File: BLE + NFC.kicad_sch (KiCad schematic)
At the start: 1 part, among them IC5 nRF52832-CIAA-G-R7

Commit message: added buck
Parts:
- added JP1: SolderJumper_3_Open, symbol Jumper:SolderJumper_3_Open
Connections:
- net at IC5.A7 (VDD_1): now also IC5.H7 (VDD_2), JP1.2 (C)
- new net +1V8: JP1.3 (B)
- new net +3V3: JP1.1 (A)
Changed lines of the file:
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@@
   (junction (at 143.51 144.78) (diameter 0) (color 0 0 0 0)
   )
+  (junction (at 133.35 43.18) (diameter 0) (color 0 0 0 0)
+  )
   (junction (at 151.13 144.78) (diameter 0) (color 0 0 0 0)
   )
+  (wire (pts (xy 138.43 36.83) (xy 146.05 36.83))
+    (stroke (width 0) (type default))
+  )
   (wire (pts (xy 151.13 142.24) (xy 151.13 144.78))
     (stroke (width 0) (type default))
@@
     (stroke (width 0) (type default))
   )
+  (wire (pts (xy 135.89 43.18) (xy 135.89 45.72))
+    (stroke (width 0) (type default))
+  )
   (wire (pts (xy 143.51 144.78) (xy 143.51 147.32))
     (stroke (width 0) (type default))
   )
+  (wire (pts (xy 128.27 36.83) (xy 120.65 36.83))
+    (stroke (width 0) (type default))
+  )
+  (wire (pts (xy 146.05 26.67) (xy 146.05 36.83))
+    (stroke (width 0) (type default))
+  )
+  (wire (pts (xy 133.35 45.72) (xy 133.35 43.18))
+    (stroke (width 0) (type default))
+  )
   (wire (pts (xy 151.13 144.78) (xy 153.67 144.78))
     (stroke (width 0) (type default))
   )
+  (wire (pts (xy 120.65 26.67) (xy 120.65 36.83))
+    (stroke (width 0) (type default))
+  )
   (wire (pts (xy 153.67 142.24) (xy 153.67 144.78))
     (stroke (width 0) (type default))
   )
+  (wire (pts (xy 133.35 43.18) (xy 135.89 43.18))
+    (stroke (width 0) (type default))
+  )
   (wire (pts (xy 146.05 142.24) (xy 146.05 144.78))
+    (stroke (width 0) (type default))
+  )
+  (wire (pts (xy 133.35 40.64) (xy 133.35 43.18))
     (stroke (width 0) (type default))
   )
@@
         )
         (path "/017c50c6-333c-4d31-ad5a-278994a09b14/3720f3b4-03b0-4b33-b5d9-366640292599"
-          (reference "IC5") (unit 1)
+          (reference "IC6") (unit 1)
         )
       )
@@
   (symbol (lib_id "power:GND") (at 143.51 147.32 0) (unit 1)
     (in_bom yes) (on_board yes) (dnp no) (fields_autoplaced)
-    (property "Reference" "#PWR042" (at 143.51 153.67 0)
+    (property "Reference" "#PWR044" (at 143.51 153.67 0)
       (effects (font (size 1.27 1.27)) hide)
     )
@@
       (project "armband"
         (path "/017c50c6-333c-4d31-ad5a-278994a09b14/3720f3b4-03b0-4b33-b5d9-366640292599"
-          (reference "#PWR042") (unit 1)
-        )
-      )
+          (reference "#PWR044") (unit 1)
+        )
+      )
+    )
+  )
+  (symbol (lib_id "power:+1V8") (at 146.05 26.67 0) (unit 1)
+    (in_bom yes) (on_board yes) (dnp no) (fields_autoplaced)
+    (property "Reference" "#PWR014" (at 146.05 30.48 0)
+      (effects (font (size 1.27 1.27)) hide)
+    )
+    (property "Value" "+1V8" (at 146.05 22.86 0)
+      (effects (font (size 1.27 1.27)))
+    )
+    (property "Footprint" "" (at 146.05 26.67 0)
+      (effects (font (size 1.27 1.27)) hide)
+    )
+    (property "Datasheet" "" (at 146.05 26.67 0)
+      (effects (font (size 1.27 1.27)) hide)
+    )
+    (pin "1")
+    (instances
+      (project "armband"
+        (path "/017c50c6-333c-4d31-ad5a-278994a09b14/2935dd4b-68c9-428b-bdab-ba656d5b03fa"
+          (reference "#PWR014") (unit 1)
+        )
+        (path "/017c50c6-333c-4d31-ad5a-278994a09b14/3720f3b4-03b0-4b33-b5d9-366640292599"
+          (reference "#PWR051") (unit 1)
+        )
+      )
+    )
+  )
+  (symbol (lib_id "power:+3V3") (at 120.65 26.67 0) (unit 1)
+    (in_bom yes) (on_board yes) (dnp no) (fields_autoplaced)
+    (property "Reference" "#PWR019" (at 120.65 30.48 0)
+      (effects (font (size 1.27 1.27)) hide)
+    )
+    (property "Value" "+3V3" (at 120.65 22.86 0)
+      (effects (font (size 1.27 1.27)))
+    )
+    (property "Footprint" "" (at 120.65 26.67 0)
+      (effects (font (size 1.27 1.27)) hide)
+    )
+    (property "Datasheet" "" (at 120.65 26.67 0)
+      (effects (font (size 1.27 1.27)) hide)
+    )
+    (pin "1")
+    (instances
+      (project "armband"
+        (path "/017c50c6-333c-4d31-ad5a-278994a09b14/2935dd4b-68c9-428b-bdab-ba656d5b03fa"
+          (reference "#PWR019") (unit 1)
+        )
+        (path "/017c50c6-333c-4d31-ad5a-278994a09b14/3720f3b4-03b0-4b33-b5d9-366640292599"
+          (reference "#PWR017") (unit 1)
+        )
+      )
+    )
+  )
+  (symbol (lib_id "Jumper:SolderJumper_3_Open") (at 133.35 36.83 0) (unit 1)
+    (in_bom yes) (on_board yes) (dnp no) (fields_autoplaced)
+    (property "Reference" "JP1" (at 133.35 31.75 0)
+      (effects (font (size 1.27 1.27)))
+    )
+    (property "Value" "SolderJumper_3_Open" (at 133.35 34.29 0)
+      (effects (font (size 1.27 1.27)))
+    )
+    (property "Footprint" "" (at 133.35 36.83 0)
+      (effects (font (size 1.27 1.27)) hide)
+    )
+    (property "Datasheet" "~" (at 133.35 36.83 0)
+      (effects (font (size 1.27 1.27)) hide)
+    )
+    (pin "1")
+    (pin "2")
+    (pin "3")
+    (instances
+      (project "armband"
+        (path "/017c50c6-333c-4d31-ad5a-278994a09b14/2935dd4b-68c9-428b-bdab-ba656d5b03fa"
+          (reference "JP1") (unit 1)
+        )
+        (path "/017c50c6-333c-4d31-ad5a-278994a09b14/3720f3b4-03b0-4b33-b5d9-366640292599"
+          (reference "JP2") (unit 1)
+        )
+      )

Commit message: cleaned up symbol fields table and removed unused or duplicate fields.
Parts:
- IC5: MFN (none) -> 949-NRF52832CIAAG-R7; Manufacturer_Name Nordic Semiconductor -> (none); Manufacturer_Part_Number nRF52832-CIAA-G-R7 -> (none); Mouser Part Number 949-NRF52832CIAAG-R7 -> (none); Mouser Price/Stock https://www.mouser.co.uk/ProductDetail/Nordic-Semiconductor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 -> (none)
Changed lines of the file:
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@@
       (effects (font (size 1.27 1.27)) (justify left top) hide)
     )
-    (property "Mouser Part Number" "949-NRF52832CIAAG-R7" (at 172.72 566.04 0)
-      (effects (font (size 1.27 1.27)) (justify left top) hide)
-    )
-    (property "Mouser Price/Stock" "https://www.mouser.co.uk/ProductDetail/Nordic-Semiconductor/nRF52832-CIAA-G-R7?qs=TCDPyi3sCW0%252B18bmEBENMQ%3D%3D" (at 172.72 666.04 0)
-      (effects (font (size 1.27 1.27)) (justify left top) hide)
-    )
-    (property "Manufacturer_Name" "Nordic Semiconductor" (at 172.72 766.04 0)
-      (effects (font (size 1.27 1.27)) (justify left top) hide)
-    )
-    (property "Manufacturer_Part_Number" "nRF52832-CIAA-G-R7" (at 172.72 866.04 0)
-      (effects (font (size 1.27 1.27)) (justify left top) hide)
+    (property "MFN" "949-NRF52832CIAAG-R7" (at 120.65 71.12 0)
+      (effects (font (size 1.27 1.27)) hide)
     )
     (pin "A1")
@@
         )
         (path "/017c50c6-333c-4d31-ad5a-278994a09b14/3720f3b4-03b0-4b33-b5d9-366640292599"
-          (reference "IC6") (unit 1)
+          (reference "IC9") (unit 1)
         )
       )
@@
   (symbol (lib_id "power:GND") (at 143.51 147.32 0) (unit 1)
     (in_bom yes) (on_board yes) (dnp no) (fields_autoplaced)
-    (property "Reference" "#PWR044" (at 143.51 153.67 0)
+    (property "Reference" "#PWR067" (at 143.51 153.67 0)
       (effects (font (size 1.27 1.27)) hide)
     )
@@
       (project "armband"
         (path "/017c50c6-333c-4d31-ad5a-278994a09b14/3720f3b4-03b0-4b33-b5d9-366640292599"
-          (reference "#PWR044") (unit 1)
+          (reference "#PWR067") (unit 1)
         )
       )
@@
         )
         (path "/017c50c6-333c-4d31-ad5a-278994a09b14/3720f3b4-03b0-4b33-b5d9-366640292599"
-          (reference "#PWR051") (unit 1)
+          (reference "#PWR066") (unit 1)
         )
       )
@@
         )
         (path "/017c50c6-333c-4d31-ad5a-278994a09b14/3720f3b4-03b0-4b33-b5d9-366640292599"
-          (reference "#PWR017") (unit 1)
+          (reference "#PWR065") (unit 1)
         )
       )

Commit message: Add nRF base layout
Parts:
- added C25 (x2): 100n 16V, Capacitor_SMD:C_0402_1005Metric, symbol Device:C_Small
- added C25 (x2): 12pF, Capacitor_SMD:C_0402_1005Metric, symbol Device:C_Small
- added C25 (x2): 100pF, Capacitor_SMD:C_0402_1005Metric, symbol Device:C_Small
- added C8: 4u7 6.3V, Capacitor_SMD:C_0402_1005Metric, symbol Device:C_Small
- added C8: 1u 6.3V, Capacitor_SMD:C_0201_0603Metric, symbol Device:C_Small
- added L4, L6: 10uH, symbol Device:L_Small
- added L5: 15uH, symbol Device:L_Small
- added Y1: Crystal, symbol Device:Crystal
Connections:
- net GND: now also C25.2, C25.2, C25.2, C25.2, C8.1, C8.2
- net at IC5.A1 (XC2): now also C25.1
- net DEC2: now reaches IC5.A2 (DEC2)
- net DEC2: now also C25.1
- net DEC4: now reaches IC5.A6 (DEC4)
- net DEC4: now also C8.1, L5.1
- net at IC5.A7 (VDD_1), IC5.H7 (VDD_2), JP1.2 (C): now also C25.1, C8.2
- net at IC5.B2 (XC1): now also C25.2
- net at IC5.B6 (DCC): now also L4.2
- net at IC5.B7 (DEC1): now also C25.1
- net DEC3: now reaches IC5.C2 (DEC3)
- net DEC3: now also C25.1
- net BT_ANT: now reaches IC5.D1 (ANT)
- net BT_ANT: now also L6.1
- net NFC_ANT2: now reaches IC5.G5 (NFC2_/P0.10)
- net NFC_ANT1: now reaches IC5.G6 (NFC1/P0.09)
- new net: C25.2, Y1.1
- new net: C25.1, Y1.2
- new net: L4.1, L5.2

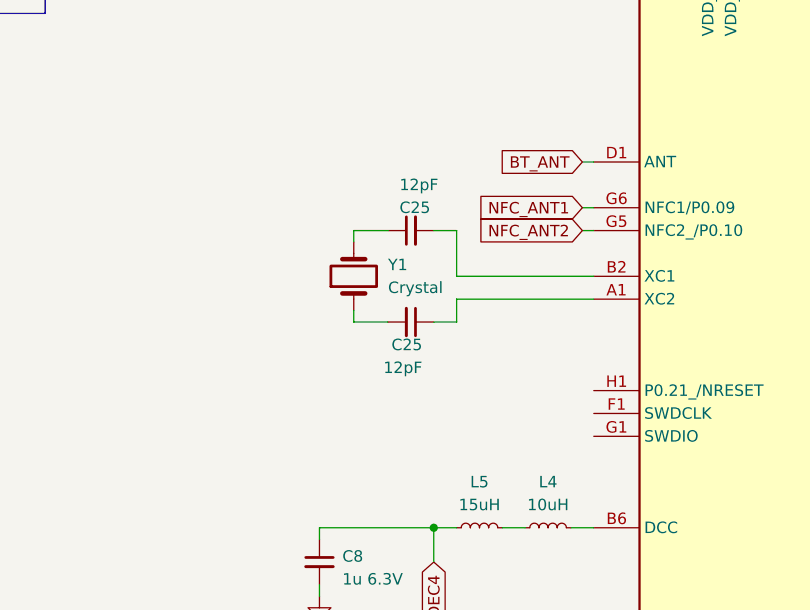
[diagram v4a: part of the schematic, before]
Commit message: added XTAL to nrf chip
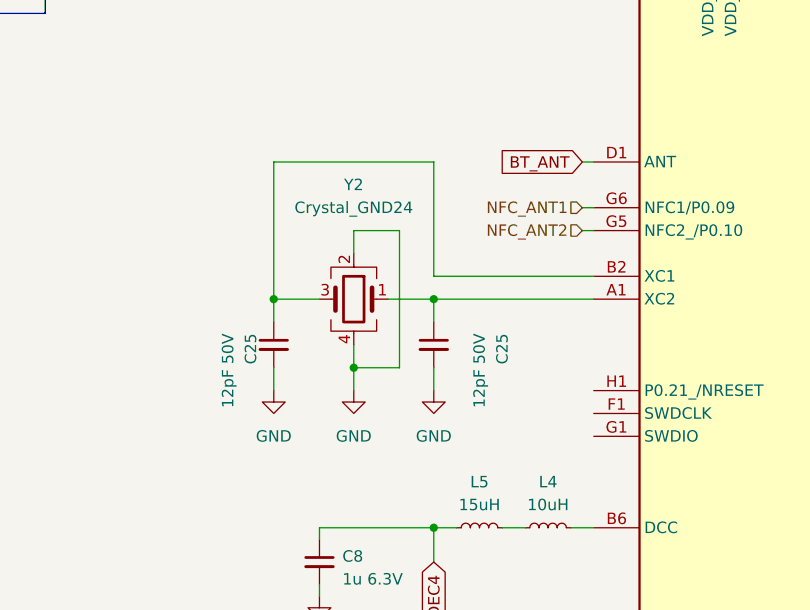
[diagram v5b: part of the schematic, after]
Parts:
- removed Y1: Crystal, symbol Device:Crystal
- added Y2: Crystal_GND24, ARMband:CX2016SA, symbol Device:Crystal_GND24
- C25: value 12pF -> 12pF 50V; footprint Capacitor_SMD:C_0402_1005Metric -> Capacitor_SMD:C_0201_0603Metric; MFN (none) -> 603-AC0201JNPO9BN120
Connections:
- net GND: now also C25.2, C25.2, Y2.2, Y2.4
- net at C25.1: now also IC5.B2 (XC1), Y2.3
- net at C25.1, IC5.A1 (XC2): now also Y2.1
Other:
- moved on the sheet: C25

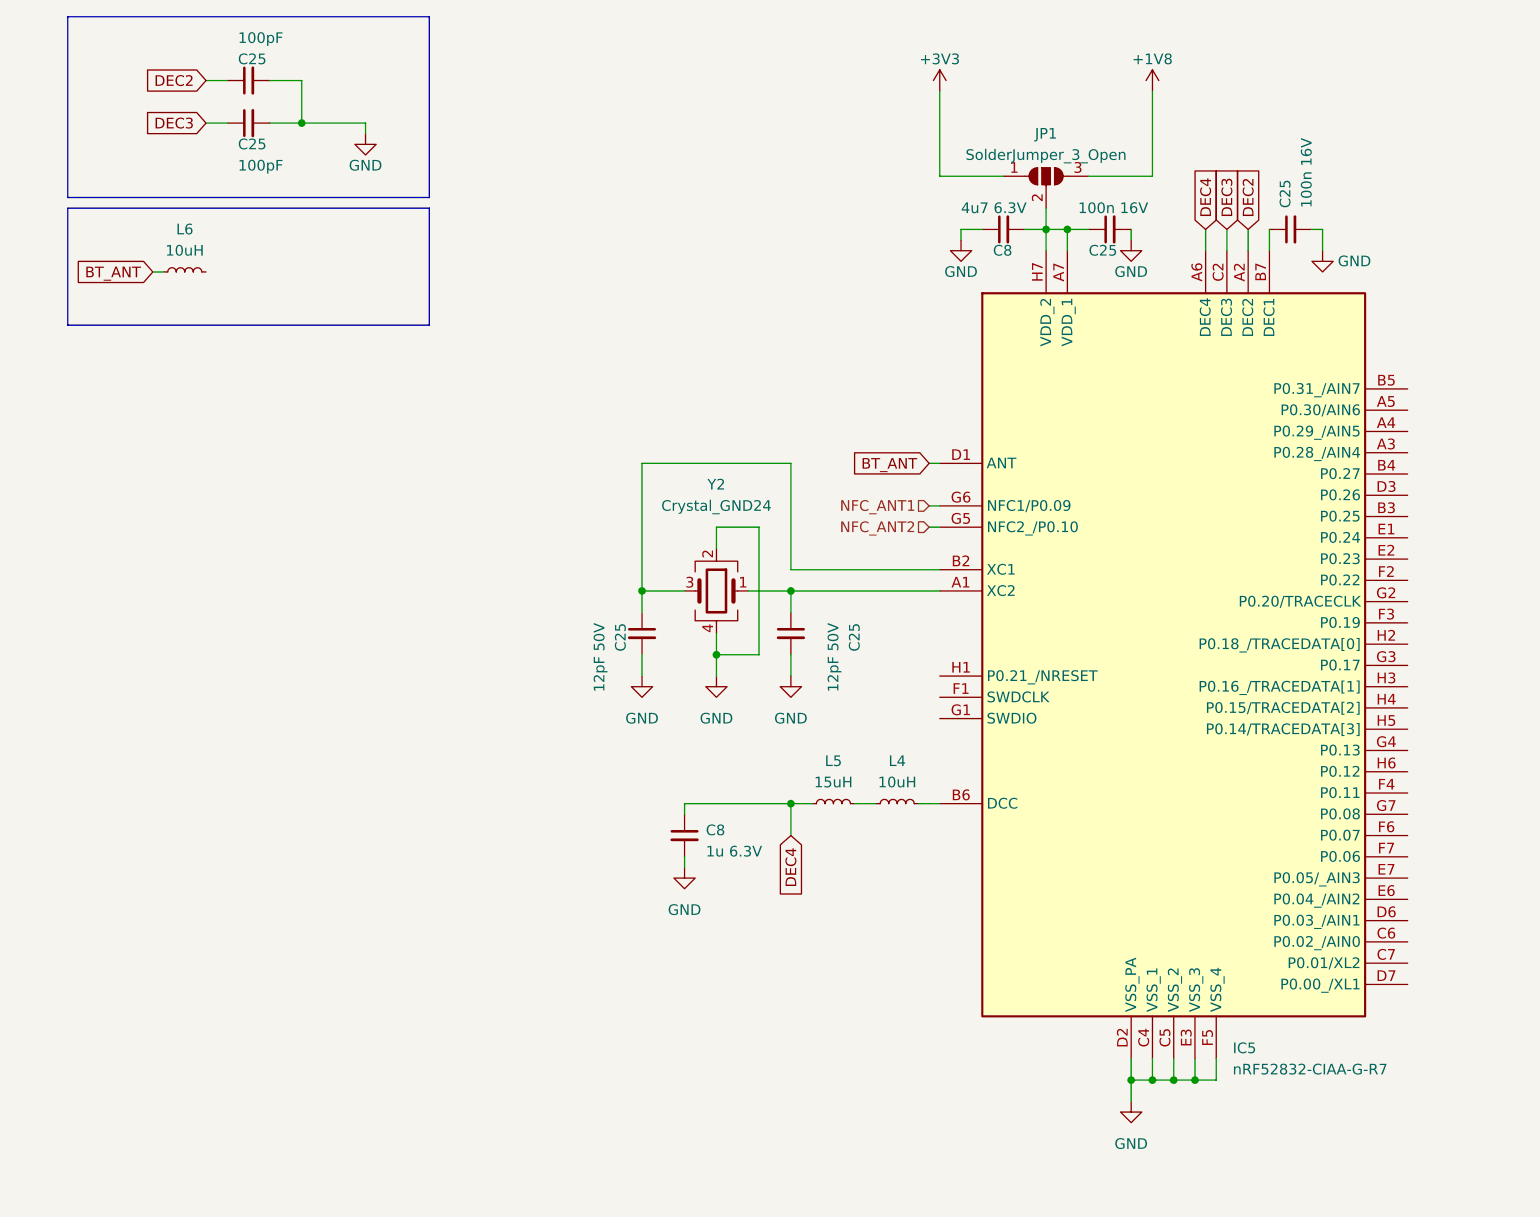
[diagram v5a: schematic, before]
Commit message: updated BLE + NFC.kicad_sch
- added antenna footprint
- added impedance matching
- added inductors on DCC pin
- changed various symbol values to match conventions (e.g. 0.9uH -> 0u9)
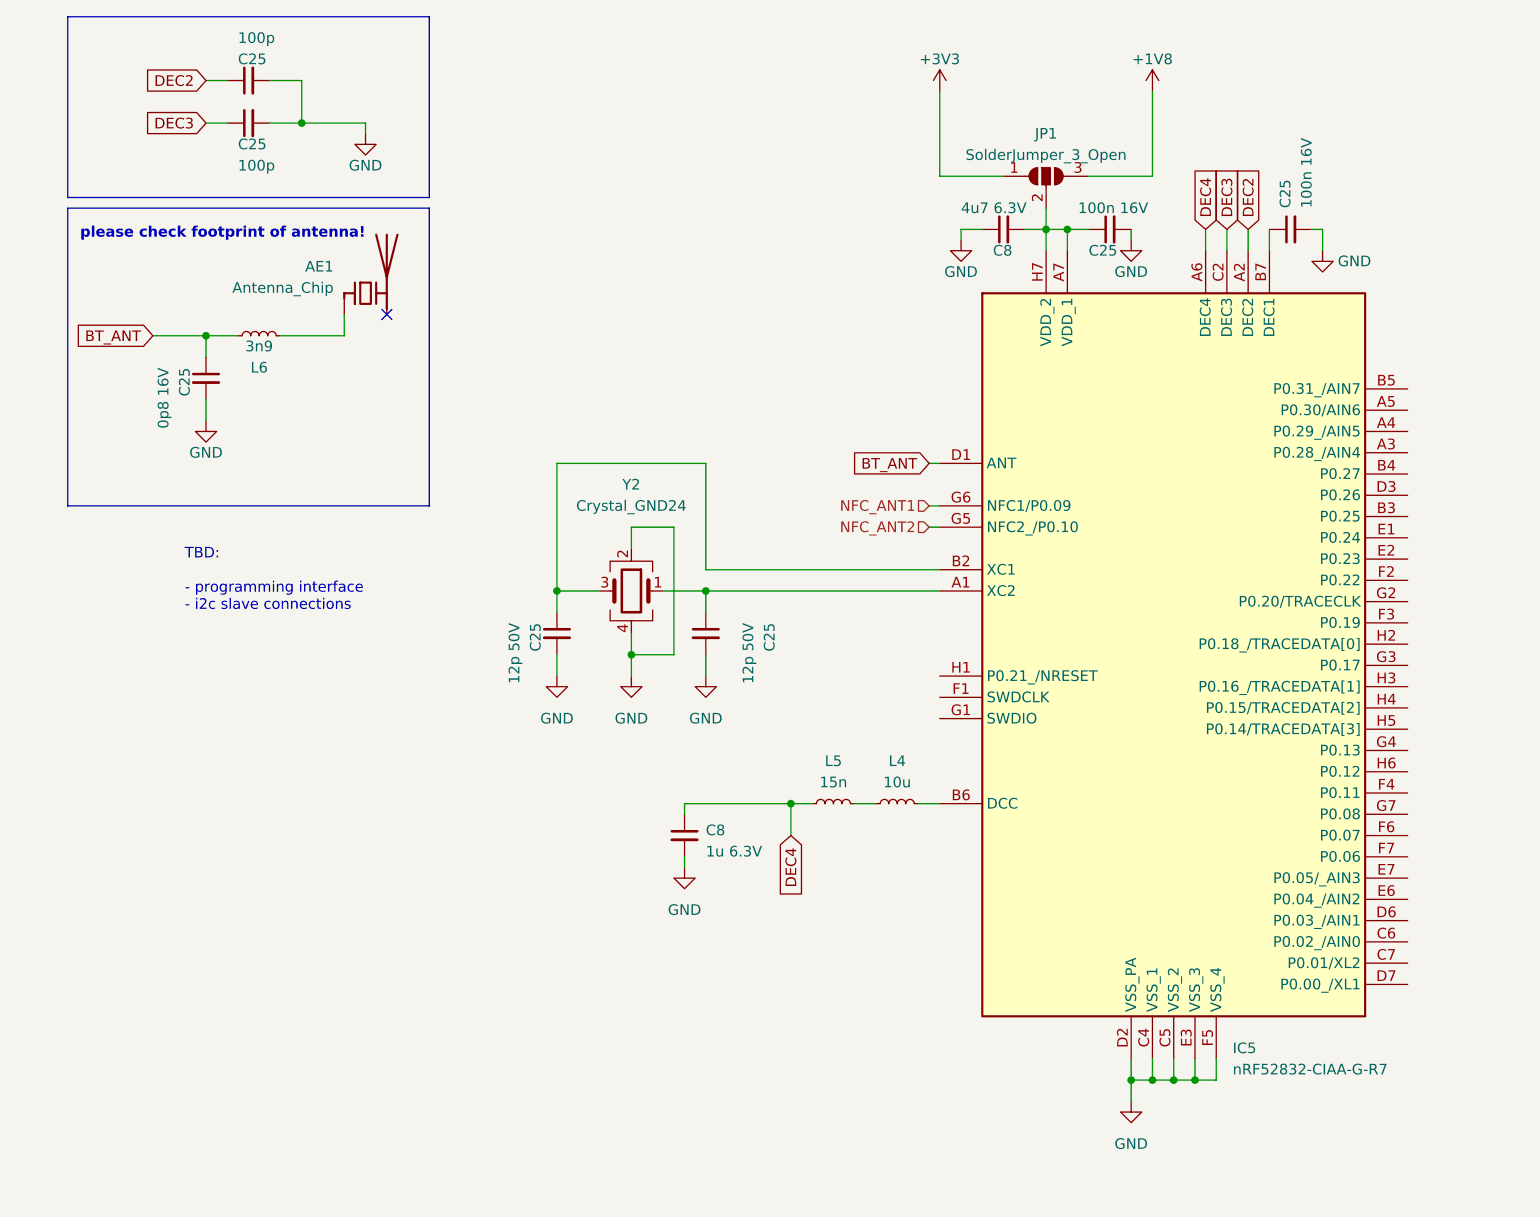
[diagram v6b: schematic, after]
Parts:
- added AE1: Antenna_Chip, ARMband:ST0147-00-011-A, symbol Device:Antenna_Chip
- added C25: 0p8 16V, Capacitor_SMD:C_0402_1005Metric, symbol Device:C_Small
- C25: value 12pF 50V -> 12p 50V
- C25: value 100pF -> 100p
- L4: value 10uH -> 10u; footprint (none) -> Inductor_SMD:L_0603_1608Metric; MFN (none) -> 810-MLZ1608E100MT
- L5: value 15uH -> 15n; footprint (none) -> Inductor_SMD:L_0201_0603Metric; MFN (none) -> 81-LQP03TG15NH02D
- L6: value 10uH -> 3n9; footprint (none) -> Inductor_SMD:L_0402_1005Metric; MFN (none) -> 81-LQG15HZ3N9S02D
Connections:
- net BT_ANT: now also L6.2, C25.1; no longer L6.1
- net GND: now also C25.2
- new net: AE1.1 (FEED), L6.1
- no-connect marks 0 -> 1
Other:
- note added: "TBD: - programming interface - i2c slave connections"
- note added: "please check footprint of antenna!"
- moved on the sheet: C25, L6, Y2
